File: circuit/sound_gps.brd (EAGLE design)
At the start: 64.2 x 56 mm, 12 parts, among them CON1 MA02-1, IC1 7805TV

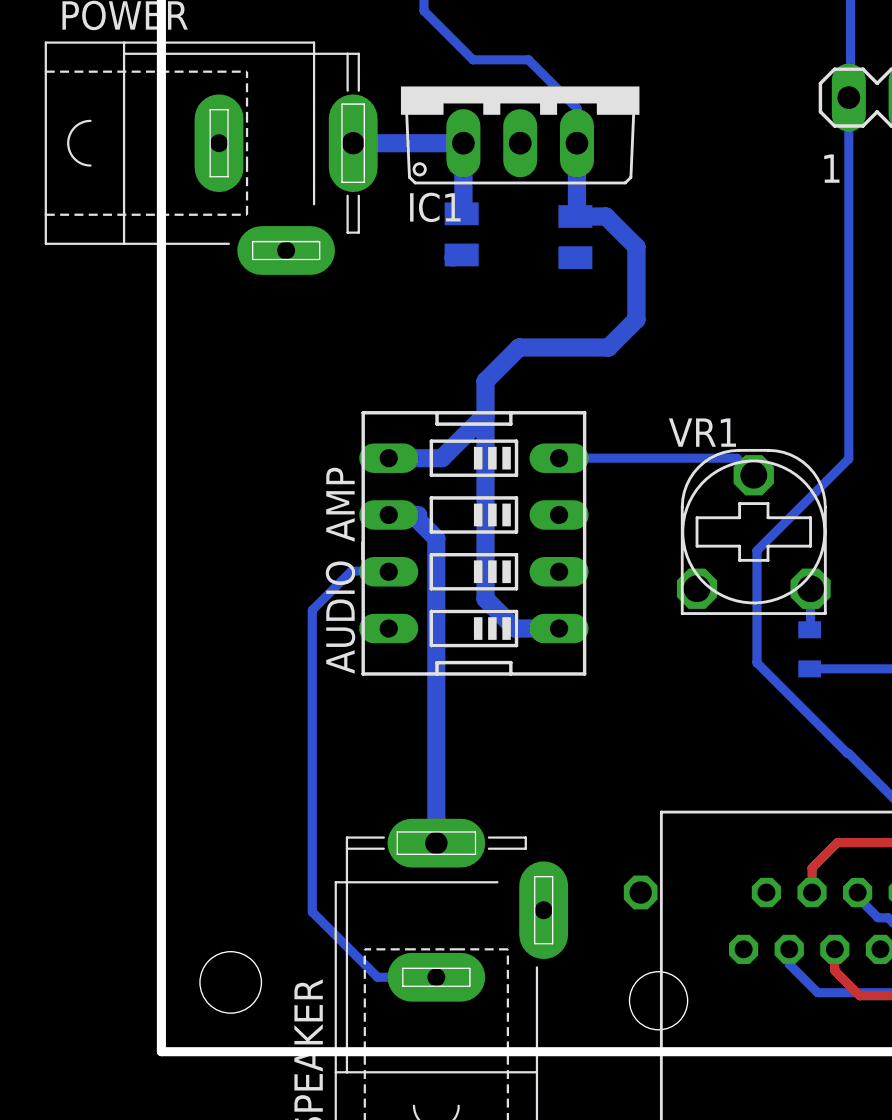
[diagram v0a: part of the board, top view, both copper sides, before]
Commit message: スイッチを追加した
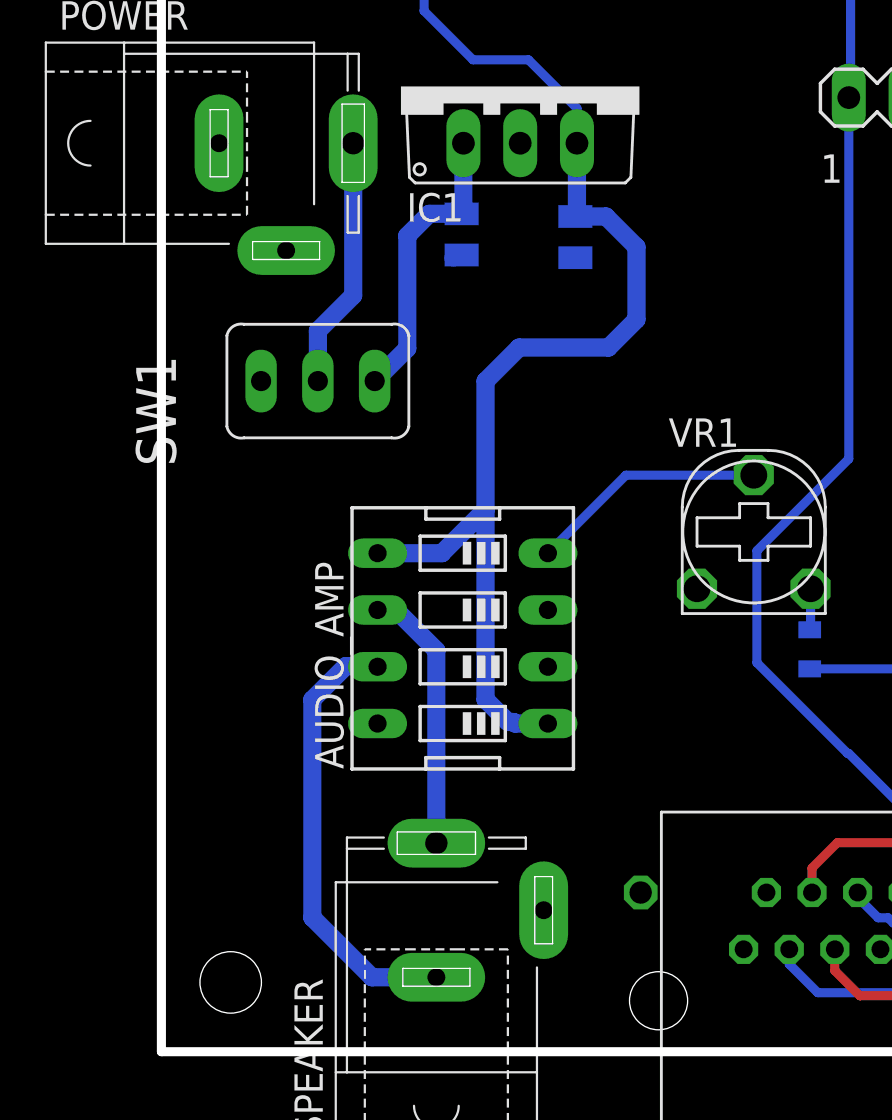
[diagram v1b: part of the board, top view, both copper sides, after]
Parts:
- added SW1: TOGGLESW_SLIM, Passive_Robotech:TOGGLESW_SLIM
- moved AUDIO_AMP 4.28 mm to (13.5, 18.5)
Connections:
- new net N$3: C1.1, IC1.1, SW1.3
- net +12V: now also SW1.2; no longer C1.1, IC1.1
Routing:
- net N$3: track 0.00 -> 13.1 mm
- net AUDIO_NOUT: track 24.4 -> 20.0 mm
- net AUDIO_POUT: track 16.4 -> 12.0 mm
- net +5V: track 54.2 -> 58.6 mm
- net +12V: track 8.12 -> 11.3 mm
- net N$1: track 9.02 -> 10.7 mm
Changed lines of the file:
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@@
 <element name="C1" library="Passive_Robotech" package="2012-C" value="0.33u" x="13.43" y="36.56" rot="MR270"/>
 <element name="C2" library="Passive_Robotech" package="2012-C" value="0.1u" x="18.52" y="36.44" rot="MR270"/>
-<element name="AUDIO_AMP" library="special" package="EDG-04" value="" x="13.98" y="22.74" rot="R90"/>
+<element name="AUDIO_AMP" library="special" package="EDG-04" value="" x="13.48" y="18.49" rot="R90"/>
 <element name="SYNC0" library="Connector_Robotech" package="AKI-RJ45-CAN" value="AKI-RJ45-CAN" x="29.49" y="4.58"/>
 <element name="SYNC1" library="Connector_Robotech" package="AKI-RJ45-CAN" value="AKI-RJ45-CAN" x="49.29" y="4.58"/>
@@
 <element name="VR1" library="Passive_Robotech" package="VR-637A" value="20k" x="26.5" y="23.25"/>
 <element name="R1" library="Passive_Robotech" package="1608" value="10k" x="29" y="18" rot="MR270"/>
+<element name="SW1" library="Passive_Robotech" package="TOGGLESW_SLIM" value="TOGGLESW_SLIM" x="7" y="30" rot="R90"/>
 </elements>
 <signals>
 <signal name="+12V">
-<contactref element="IC1" pad="1"/>
-<contactref element="C1" pad="1"/>
 <contactref element="POWER" pad="3"/>
-<wire x1="13.51" y1="40.64" x2="13.51" y2="37.5607" width="0.8128" layer="16"/>
-<wire x1="13.51" y1="37.5607" x2="13.43" y2="37.4807" width="0.8128" layer="16"/>
-<wire x1="8.58" y1="40.64" x2="13.51" y2="40.64" width="0.8128" layer="16"/>
+<contactref element="SW1" pad="2"/>
+<wire x1="8.58" y1="40.64" x2="8.58" y2="33.83" width="0.8128" layer="16"/>
+<wire x1="8.58" y1="33.83" x2="7" y2="32.25" width="0.8128" layer="16"/>
+<wire x1="7" y1="32.25" x2="7" y2="30" width="0.8128" layer="16"/>
 </signal>
 <signal name="+5V">
@@
 <wire x1="20" y1="31.5" x2="16" y2="31.5" width="0.8128" layer="16"/>
 <wire x1="16" y1="31.5" x2="14.5" y2="30" width="0.8128" layer="16"/>
-<wire x1="14.5" y1="30" x2="14.5" y2="28.5" width="0.8128" layer="16"/>
-<wire x1="14.5" y1="28.5" x2="14.5" y2="20.25" width="0.8128" layer="16"/>
-<wire x1="14.5" y1="20.25" x2="15.82" y2="18.93" width="0.8128" layer="16"/>
-<wire x1="17.79" y1="18.93" x2="15.82" y2="18.93" width="0.8128" layer="16"/>
-<wire x1="10.17" y1="26.55" x2="12.55" y2="26.55" width="0.8128" layer="16"/>
-<wire x1="12.55" y1="26.55" x2="14.5" y2="28.5" width="0.8128" layer="16"/>
+<wire x1="14.5" y1="30" x2="14.5" y2="24.25" width="0.8128" layer="16"/>
+<wire x1="14.5" y1="24.25" x2="14.5" y2="15.75" width="0.8128" layer="16"/>
+<wire x1="17.29" y1="14.68" x2="15.82" y2="14.68" width="0.8128" layer="16"/>
+<wire x1="15.82" y1="14.68" x2="15.75" y2="14.75" width="0.8128" layer="16"/>
+<wire x1="15.75" y1="14.75" x2="15.5" y2="14.75" width="0.8128" layer="16"/>
+<wire x1="15.5" y1="14.75" x2="14.5" y2="15.75" width="0.8128" layer="16"/>
+<wire x1="9.67" y1="22.3" x2="12.55" y2="22.3" width="0.8128" layer="16"/>
+<wire x1="12.55" y1="22.3" x2="14.5" y2="24.25" width="0.8128" layer="16"/>
 </signal>
 <signal name="GND">
@@
 <contactref element="AUDIO_AMP" pad="7"/>
 <contactref element="SPEAKER" pad="1"/>
-<wire x1="6.75" y1="6.25" x2="6.75" y2="19.75" width="0.4064" layer="16"/>
-<wire x1="6.75" y1="19.75" x2="8.5" y2="21.5" width="0.4064" layer="16"/>
-<wire x1="8.5" y1="21.5" x2="10.14" y2="21.5" width="0.4064" layer="16"/>
-<wire x1="10.14" y1="21.5" x2="10.17" y2="21.47" width="0.4064" layer="16"/>
-<wire x1="12.3" y1="3.33" x2="9.67" y2="3.33" width="0.4064" layer="16"/>
-<wire x1="9.67" y1="3.33" x2="6.75" y2="6.25" width="0.4064" layer="16"/>
+<wire x1="12.3" y1="3.33" x2="9.42" y2="3.33" width="0.8128" layer="16"/>
+<wire x1="9.42" y1="3.33" x2="6.75" y2="6" width="0.8128" layer="16"/>
+<wire x1="6.75" y1="6" x2="6.75" y2="15.75" width="0.8128" layer="16"/>
+<wire x1="6.75" y1="15.75" x2="8.25" y2="17.25" width="0.8128" layer="16"/>
+<wire x1="8.25" y1="17.25" x2="9.64" y2="17.25" width="0.8128" layer="16"/>
+<wire x1="9.64" y1="17.25" x2="9.67" y2="17.22" width="0.8128" layer="16"/>
 </signal>
 <signal name="AUDIO_POUT">
 <contactref element="AUDIO_AMP" pad="6"/>
 <contactref element="SPEAKER" pad="3"/>
-<wire x1="10.17" y1="24.01" x2="11.25" y2="24.01" width="0.8128" layer="16"/>
-<wire x1="11.25" y1="24.01" x2="11.49" y2="24.01" width="0.8128" layer="16"/>
-<wire x1="12.3" y1="9.33" x2="12.3" y2="22.96" width="0.8128" layer="16"/>
-<wire x1="12.3" y1="22.96" x2="11.25" y2="24.01" width="0.8128" layer="16"/>
+<wire x1="9.67" y1="19.76" x2="10.49" y2="19.76" width="0.8128" layer="16"/>
+<wire x1="10.49" y1="19.76" x2="12.3" y2="17.95" width="0.8128" layer="16"/>
+<wire x1="12.3" y1="9.33" x2="12.3" y2="17.95" width="0.8128" layer="16"/>
 </signal>
 <signal name="VCC-1">
@@
 <contactref element="AUDIO_AMP" pad="4"/>
 <contactref element="VR1" pad="BR"/>
-<wire x1="17.79" y1="26.55" x2="25.74" y2="26.55" width="0.4064" layer="16"/>
-<wire x1="25.74" y1="26.55" x2="26.5" y2="25.79" width="0.4064" layer="16"/>
+<wire x1="26.5" y1="25.79" x2="20.78" y2="25.79" width="0.4064" layer="16"/>
+<wire x1="20.78" y1="25.79" x2="17.29" y2="22.3" width="0.4064" layer="16"/>
 </signal>
 <signal name="N$2">
@@
 <wire x1="29.04" y1="18.915" x2="29" y2="18.875" width="0.4064" layer="16"/>
 </signal>
+<signal name="N$3">
+<contactref element="IC1" pad="1"/>
+<contactref element="C1" pad="1"/>
+<wire x1="13.51" y1="40.64" x2="13.51" y2="37.5607" width="0.8128" layer="16"/>
+<wire x1="13.51" y1="37.5607" x2="13.43" y2="37.4807" width="0.8128" layer="16"/>
+<contactref element="SW1" pad="3"/>
+<wire x1="13.43" y1="37.4807" x2="11.9807" y2="37.4807" width="0.8128" layer="16"/>
+<wire x1="11.9807" y1="37.4807" x2="11" y2="36.5" width="0.8128" layer="16"/>
+<wire x1="11" y1="36.5" x2="11" y2="31.46" width="0.8128" layer="16"/>
+<wire x1="11" y1="31.46" x2="9.54" y2="30" width="0.8128" layer="16"/>
+</signal>
 </signals>

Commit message: circuit version 2.0
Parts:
- POWER, SPEAKER: value (none) -> DCJACK-NEW-18742; device con-jack:SPC4077 -> Connector_Robotech:18742
- moved SPEAKER 4.10 mm to (12.8, 2.25)
- moved POWER 3.37 mm to (2.50, 42.0)
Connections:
- net +12V: now also POWER.P$1; no longer POWER.3
- net AUDIO_NOUT: now also SPEAKER.P$2; no longer SPEAKER.1
- net AUDIO_POUT: now also SPEAKER.P$1; no longer SPEAKER.3
- net GND: now also POWER.P$2; no longer POWER.1
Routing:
- net AUDIO_POUT: track 12.0 -> 13.5 mm
- net +12V: track 11.3 -> 12.6 mm
- net AUDIO_NOUT: track 20.0 -> 20.9 mm
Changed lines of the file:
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@@
 <element name="SYNC1" library="Connector_Robotech" package="AKI-RJ45-CAN" value="AKI-RJ45-CAN" x="49.29" y="4.58"/>
 <element name="CON1" library="Connector_Robotech" package="MA02-1" value="MA02-1" x="32.02" y="42.68"/>
-<element name="POWER" library="con-jack" package="SPC4077" value="" x="5.58" y="40.64">
-<attribute name="OC_NEWARK" value="unknown" x="5.58" y="40.64" size="1.778" layer="27" display="off"/>
-<attribute name="MF" value="" x="5.58" y="40.64" size="1.778" layer="27" display="off"/>
-<attribute name="MPN" value="" x="5.58" y="40.64" size="1.778" layer="27" display="off"/>
-<attribute name="OC_FARNELL" value="unknown" x="5.58" y="40.64" size="1.778" layer="27" display="off"/>
-</element>
-<element name="SPEAKER" library="con-jack" package="SPC4077" value="" x="12.3" y="6.33" rot="R90">
-<attribute name="OC_NEWARK" value="unknown" x="12.3" y="6.33" size="1.778" layer="27" rot="R90" display="off"/>
-<attribute name="MF" value="" x="12.3" y="6.33" size="1.778" layer="27" rot="R90" display="off"/>
-<attribute name="MPN" value="" x="12.3" y="6.33" size="1.778" layer="27" rot="R90" display="off"/>
-<attribute name="OC_FARNELL" value="unknown" x="12.3" y="6.33" size="1.778" layer="27" rot="R90" display="off"/>
-</element>
 <element name="VR1" library="Passive_Robotech" package="VR-637A" value="20k" x="26.5" y="23.25"/>
 <element name="R1" library="Passive_Robotech" package="1608" value="10k" x="29" y="18" rot="MR270"/>
 <element name="SW1" library="Passive_Robotech" package="TOGGLESW_SLIM" value="TOGGLESW_SLIM" x="7" y="30" rot="R90"/>
+<element name="POWER" library="Connector_Robotech" package="18742" value="DCJACK-NEW-18742" x="2.5" y="42"/>
+<element name="SPEAKER" library="Connector_Robotech" package="18742" value="DCJACK-NEW-18742" x="12.75" y="2.25" rot="R90"/>
 </elements>
 <signals>
 <signal name="+12V">
-<contactref element="POWER" pad="3"/>
 <contactref element="SW1" pad="2"/>
-<wire x1="8.58" y1="40.64" x2="8.58" y2="33.83" width="0.8128" layer="16"/>
-<wire x1="8.58" y1="33.83" x2="7" y2="32.25" width="0.8128" layer="16"/>
 <wire x1="7" y1="32.25" x2="7" y2="30" width="0.8128" layer="16"/>
+<contactref element="POWER" pad="P$1"/>
+<wire x1="8.3" y1="42" x2="8.25" y2="42" width="0.8128" layer="16"/>
+<wire x1="8.25" y1="42" x2="8.25" y2="33.5" width="0.8128" layer="16"/>
+<wire x1="8.25" y1="33.5" x2="7" y2="32.25" width="0.8128" layer="16"/>
 </signal>
 <signal name="+5V">
@@
 <contactref element="SYNC1" pad="SHIELD1"/>
 <contactref element="SYNC1" pad="SHIELD2"/>
-<contactref element="POWER" pad="1"/>
 <contactref element="SYNC1" pad="CANL"/>
 <contactref element="JP1" pad="6"/>
@@
 <contactref element="JP1" pad="39"/>
 <contactref element="JP1" pad="25"/>
+<contactref element="POWER" pad="P$2"/>
 </signal>
 <signal name="AUDIO_IN">
@@
 <signal name="AUDIO_NOUT">
 <contactref element="AUDIO_AMP" pad="7"/>
-<contactref element="SPEAKER" pad="1"/>
-<wire x1="12.3" y1="3.33" x2="9.42" y2="3.33" width="0.8128" layer="16"/>
-<wire x1="9.42" y1="3.33" x2="6.75" y2="6" width="0.8128" layer="16"/>
+<wire x1="10.5" y1="2.25" x2="6.75" y2="6" width="0.8128" layer="16"/>
 <wire x1="6.75" y1="6" x2="6.75" y2="15.75" width="0.8128" layer="16"/>
 <wire x1="6.75" y1="15.75" x2="8.25" y2="17.25" width="0.8128" layer="16"/>
 <wire x1="8.25" y1="17.25" x2="9.64" y2="17.25" width="0.8128" layer="16"/>
 <wire x1="9.64" y1="17.25" x2="9.67" y2="17.22" width="0.8128" layer="16"/>
+<contactref element="SPEAKER" pad="P$2"/>
+<wire x1="12.75" y1="2.25" x2="10.5" y2="2.25" width="0.8128" layer="16"/>
 </signal>
 <signal name="AUDIO_POUT">
 <contactref element="AUDIO_AMP" pad="6"/>
-<contactref element="SPEAKER" pad="3"/>
 <wire x1="9.67" y1="19.76" x2="10.49" y2="19.76" width="0.8128" layer="16"/>
-<wire x1="10.49" y1="19.76" x2="12.3" y2="17.95" width="0.8128" layer="16"/>
-<wire x1="12.3" y1="9.33" x2="12.3" y2="17.95" width="0.8128" layer="16"/>
+<wire x1="10.49" y1="19.76" x2="12.75" y2="17.5" width="0.8128" layer="16"/>
+<contactref element="SPEAKER" pad="P$1"/>
+<wire x1="12.75" y1="8.05" x2="12.75" y2="17.5" width="0.8128" layer="16"/>
 </signal>
 <signal name="VCC-1">

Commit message: circuit version 3.0
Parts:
- removed POWER, SPEAKER: DCJACK-NEW-18742, Connector_Robotech:18742
- added CN1: DCJACK-NEW-18742, Connector_Robotech:18742
- added J2: DCJACK, Connector_Robotech:DCJACK
- moved R1 14.5 mm to (27.6, 32.4), turned to 180 degrees
- moved VR1 9.19 mm to (20.1, 29.8), turned to 90 degrees
- moved AUDIO_AMP 6.14 mm to (8.66, 22.3), turned to 180 degrees
- moved IC1 5.75 mm to (21.4, 45.3)
- moved C1 5.03 mm to (17.3, 39.7), turned to 180 degrees
- moved SW1 1.55 mm to (6.61, 31.5)
- moved CON1 0.18 mm to (32.1, 42.5)
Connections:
- net +12V: now also CN1.P$1; no longer POWER.P$1
- net AUDIO_NOUT: now also J2.SIDE1; no longer SPEAKER.P$2
- net AUDIO_POUT: now also J2.CENTER; no longer SPEAKER.P$1
- net GND: now also CN1.P$2; no longer POWER.P$2
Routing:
- net AUDIO_IN: track 47.4 -> 33.4 mm
- net AUDIO_NOUT: track 20.9 -> 33.1 mm
- net N$1: track 10.7 -> 20.1 mm
- net +5V: track 58.6 -> 67.2 mm
- net SYNC_CLK: track 69.9 -> 76.5 mm
- net AUDIO_POUT: track 13.5 -> 7.90 mm
- net N$3: track 13.1 -> 16.3 mm
- net N$2: track 1.85 -> 4.07 mm
- net GND: track 1.96 -> 0.00 mm
